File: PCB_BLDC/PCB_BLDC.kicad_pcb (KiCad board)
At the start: 2 copper layers, 177 x 135.1 mm, 61 parts, among them J10 Conn_01x06, J11 Conn_01x07, J12 Conn_01x06, J13 Conn_01x08, J16 Conn_01x08, J17 Conn_01x10, J8 VCC_Unregulated, J9 VCC_GND, Q1 IRF4905, SW1 Rotary_Encoder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

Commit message: Main: Update PCB, Add Vias, Update Schematic, Update Netlist
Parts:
- removed J11: Conn_01x07, TerminalBlock_Phoenix:TerminalBlock_Phoenix_MKDS-1,5-7_1x07_P5.00mm_Horizontal
- removed J9: VCC_GND, Connector:Banana_Jack_1Pin
- added J1: Conn_01x08, TerminalBlock_Phoenix:TerminalBlock_Phoenix_MKDS-1,5-8_1x08_P5.00mm_Horizontal, F.Cu at (201.7, 100.6)
- C1, C2, C4: footprint Capacitor_SMD:C_1206_3216Metric_Pad1.33x1.80mm_HandSolder -> Capacitor_SMD:C_1210_3225Metric_Pad1.33x2.70mm_HandSolder
- J8: value VCC_Unregulated -> Power Terminal; footprint Connector:Banana_Jack_1Pin -> Connector:Banana_Jack_2Pin
- R3: value 100 -> 150
- turned J8 to 90 degrees
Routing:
- net GND: track 152.2 -> 158.3 mm, vias 70 -> 95
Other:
- board text added: "BLDC V1.0"

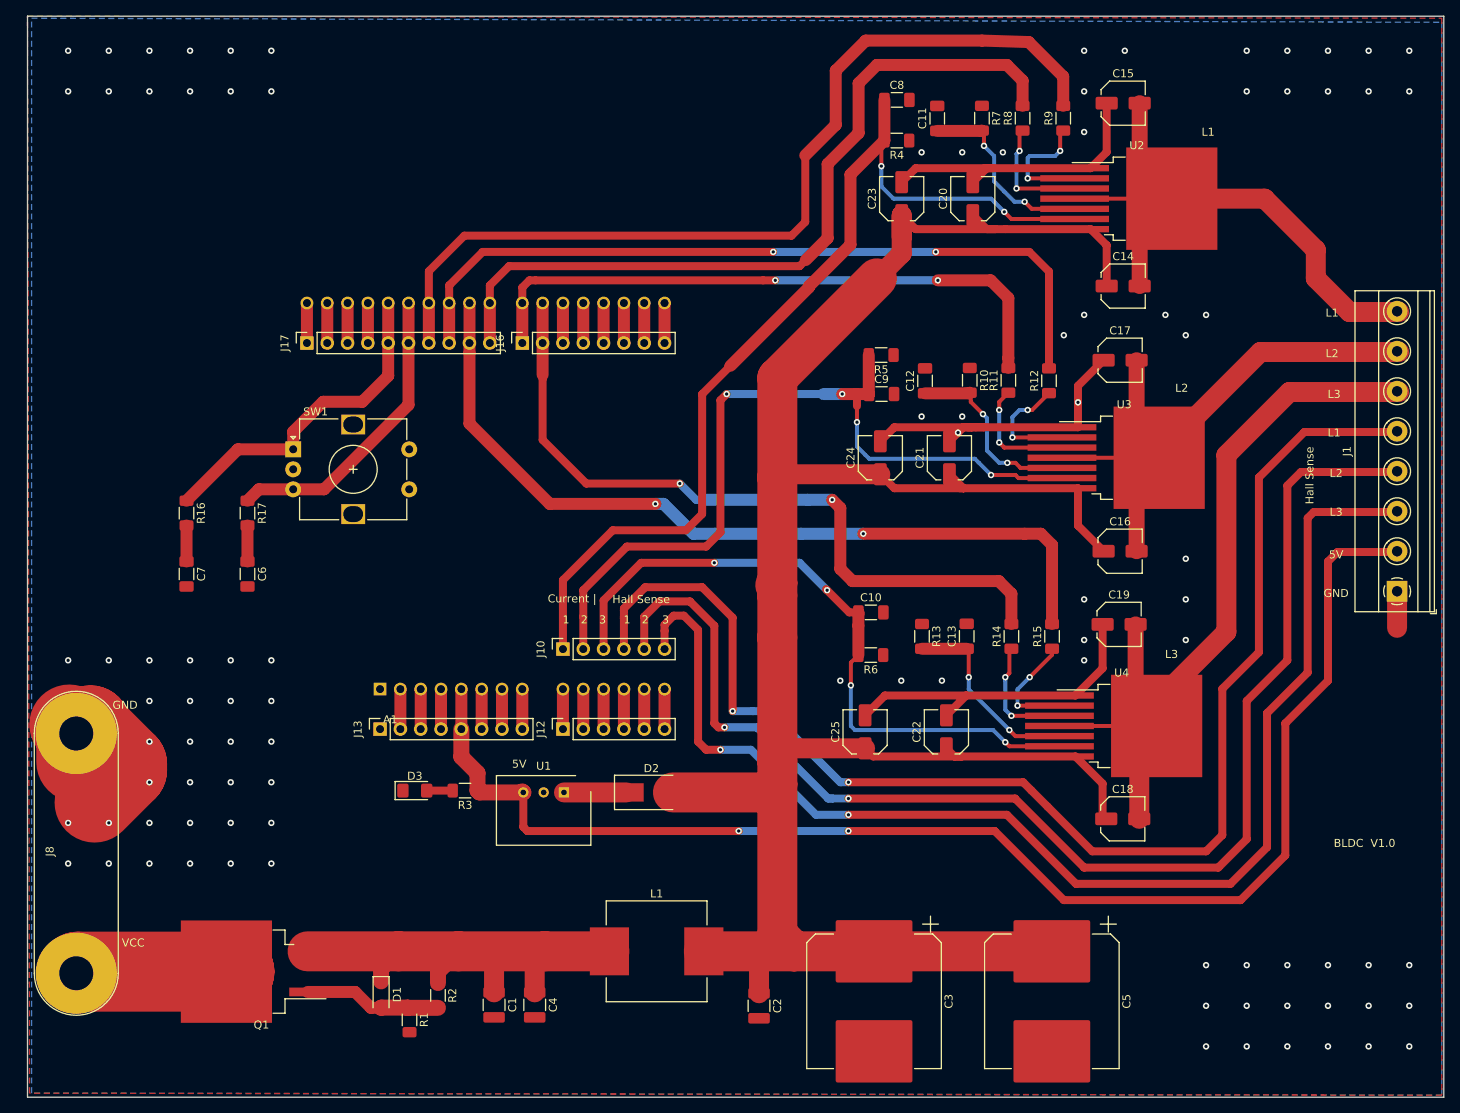
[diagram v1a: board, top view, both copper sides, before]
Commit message: Main: Update Schematic, Add Vias, RC-Filt for Hall-Sense
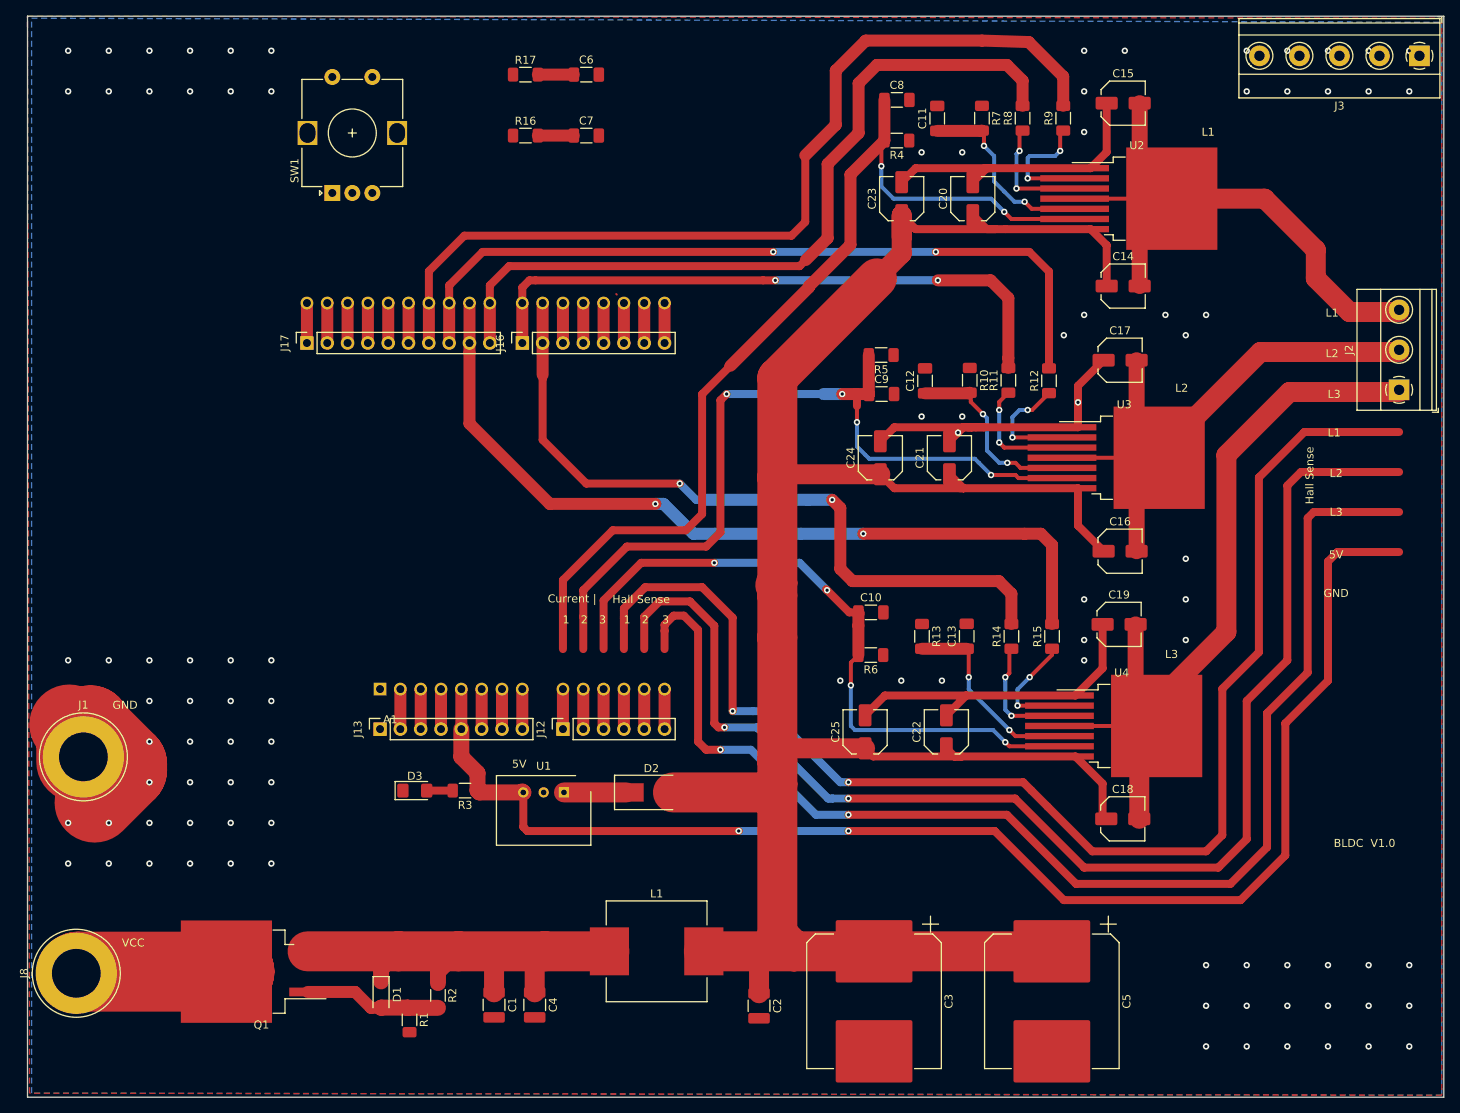
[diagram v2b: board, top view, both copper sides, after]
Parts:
- removed J10: Conn_01x06, Connector_PinSocket_2.54mm:PinSocket_1x06_P2.54mm_Vertical
- added J2: Conn_01x03, TerminalBlock_Phoenix:TerminalBlock_Phoenix_MKDS-1,5-3_1x03_P5.00mm_Horizontal, F.Cu at (201.9, 75.4)
- added J3: Conn_01x05, TerminalBlock_Phoenix:TerminalBlock_Phoenix_MKDS-1,5-5_1x05_P5.00mm_Horizontal, F.Cu at (204.5, 33.7)
- J1: value Conn_01x08 -> Power Terminal; footprint TerminalBlock_Phoenix:TerminalBlock_Phoenix_MKDS-1,5-8_1x08_P5.00mm_Horizontal -> Connector:Banana_Jack_1Pin
- J8: footprint Connector:Banana_Jack_2Pin -> Connector:Banana_Jack_1Pin
- moved J1 165.5 mm to (37.5, 121.3), turned to 0 degrees
- moved C6 75.4 mm to (100.3, 36.0), turned to 0 degrees
- moved C7 74.2 mm to (100.3, 43.6), turned to 0 degrees
- moved R17 64.9 mm to (92.7, 36.0), turned to 0 degrees
- moved R16 63.4 mm to (92.7, 43.6), turned to 0 degrees
- moved SW1 32.4 mm to (68.6, 50.8), turned to 90 degrees
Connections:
- net /Rot_A_Pull_Up renamed /D13
- net /Rot_B_Pull_Up renamed /D12
- C10 pad 1: /L3_IS -> /A2
- C8 pad 1: /L1_IS -> /A0
- C9 pad 1: /L2_IS -> /A1
- R4 pad 2: /L1_IS -> /A0
- R5 pad 2: /L2_IS -> /A1
- R6 pad 2: /L3_IS -> /A2
- U2 pad 6: /L1_IS -> /A0
- U3 pad 6: /L2_IS -> /A1
- U4 pad 6: /L3_IS -> /A2
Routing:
- net /L1_IS: track 124.9 -> 0.00 mm, vias 2 -> 0
- net /A0: track 5.00 -> 129.9 mm, vias 0 -> 2
- net /L2_IS: track 105.3 -> 0.00 mm, vias 4 -> 0
- net /A1: track 5.00 -> 110.3 mm, vias 0 -> 4
- net /L3_IS: track 86.6 -> 0.00 mm, vias 4 -> 0
- net /A2: track 5.00 -> 91.6 mm, vias 0 -> 4
- net /D13: track 42.1 -> 5.00 mm
- net /D12: track 37.8 -> 5.00 mm
- net GND: track 158.3 -> 153.7 mm, vias 95 -> 94
